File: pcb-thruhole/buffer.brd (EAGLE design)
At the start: 98 x 24 mm, 16 parts, among them IC1 LF353N, IC2 LF353N, IC3 LF353N

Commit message: fix for oopsy
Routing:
- net N$2: track 7.90 -> 0.00 mm
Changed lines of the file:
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@@
 <wire x1="30.7" y1="11.6" x2="31" y2="11.3" width="0.254" layer="16"/>
-</signal>
-<signal name="N$2">
-<wire x1="54.23" y1="17.77" x2="49.83" y2="17.77" width="0.254" layer="16"/>
-<wire x1="49.83" y1="17.77" x2="49.83" y2="14.27" width="0.254" layer="16"/>
 </signal>
 </signals>

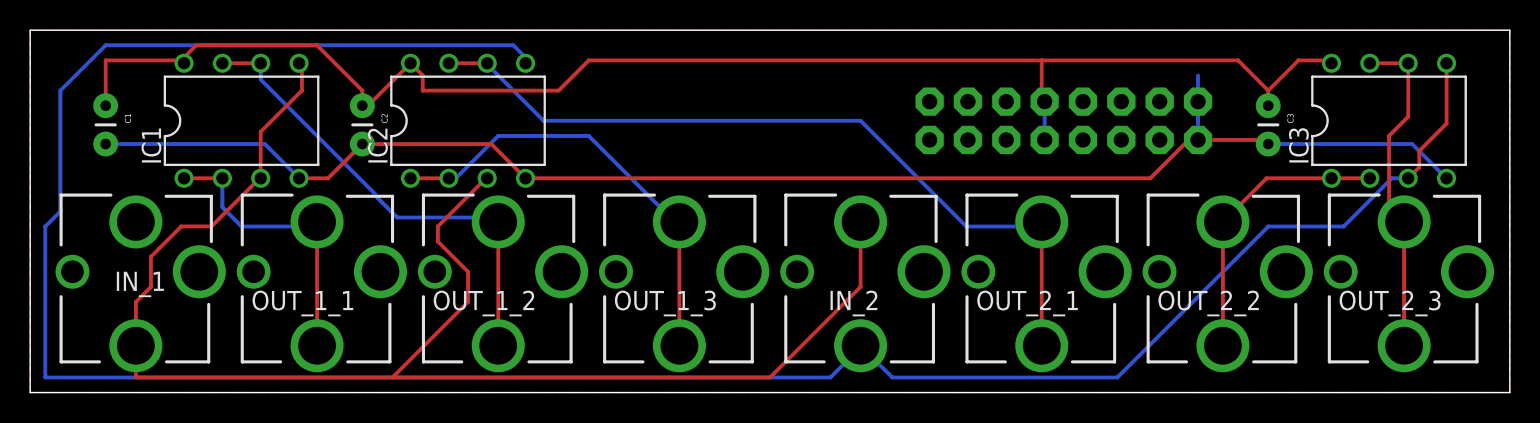
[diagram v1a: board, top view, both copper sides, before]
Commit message: moved ICs to the back so they don't hit the jacks.
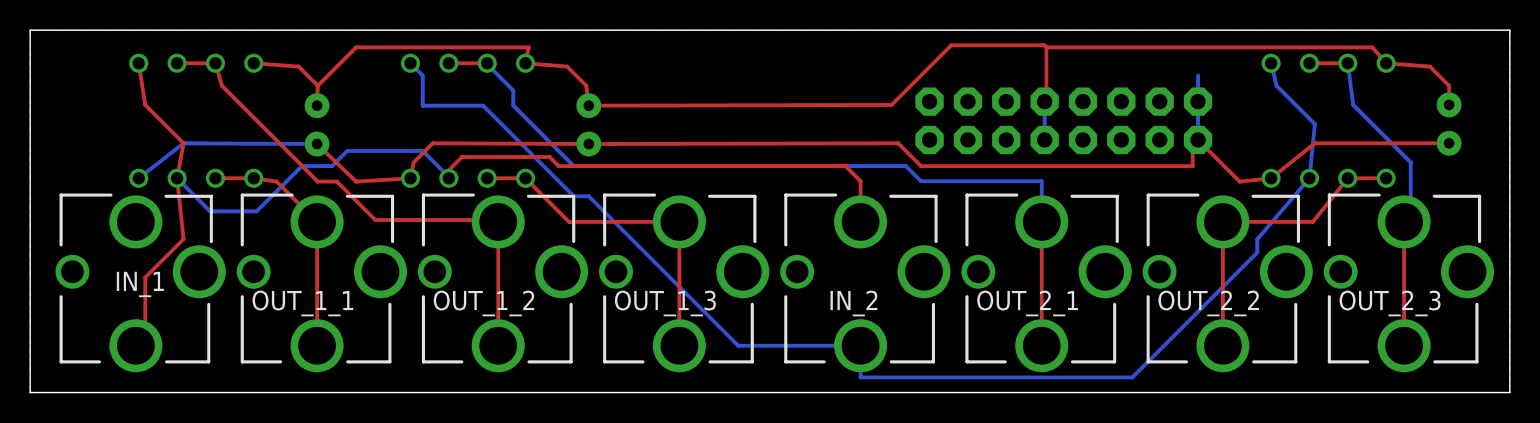
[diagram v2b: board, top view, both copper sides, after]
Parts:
- moved C2 15.0 mm to (37.0, 19.0), flipped to the bottom
- moved C1 14.0 mm to (19.0, 19.0), flipped to the bottom
- moved C3 12.0 mm to (94.0, 19.1), flipped to the bottom
- moved IC3 4.00 mm to (86.0, 18.0), flipped to the bottom
- moved IC1 3.00 mm to (11.0, 18.0), flipped to the bottom
- moved U$6 2.54 mm to (53.4, 20.2)
- flipped IC2 to the bottom
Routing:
- net N$13: track 158.4 -> 85.5 mm
- net N$10: track 98.9 -> 74.4 mm
- net N$3: track 30.4 -> 22.5 mm
- net N$1: track 19.6 -> 16.1 mm
- net +12V: track 98.6 -> 95.2 mm
- net N$4: track 31.5 -> 34.3 mm
- net N$11: track 52.4 -> 54.3 mm
- net N$15: track 19.1 -> 20.4 mm
